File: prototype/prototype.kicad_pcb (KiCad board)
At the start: 4 copper layers, 78.7 x 63.5 mm, 47 parts, among them P1 CONN_25X2, P2 CONN_25X2, P3 VGACONN, U1 MC68SEC000, U2 FLASHROM_512K_16, U3 RAM_512K_16, U4 RAM_512K_16

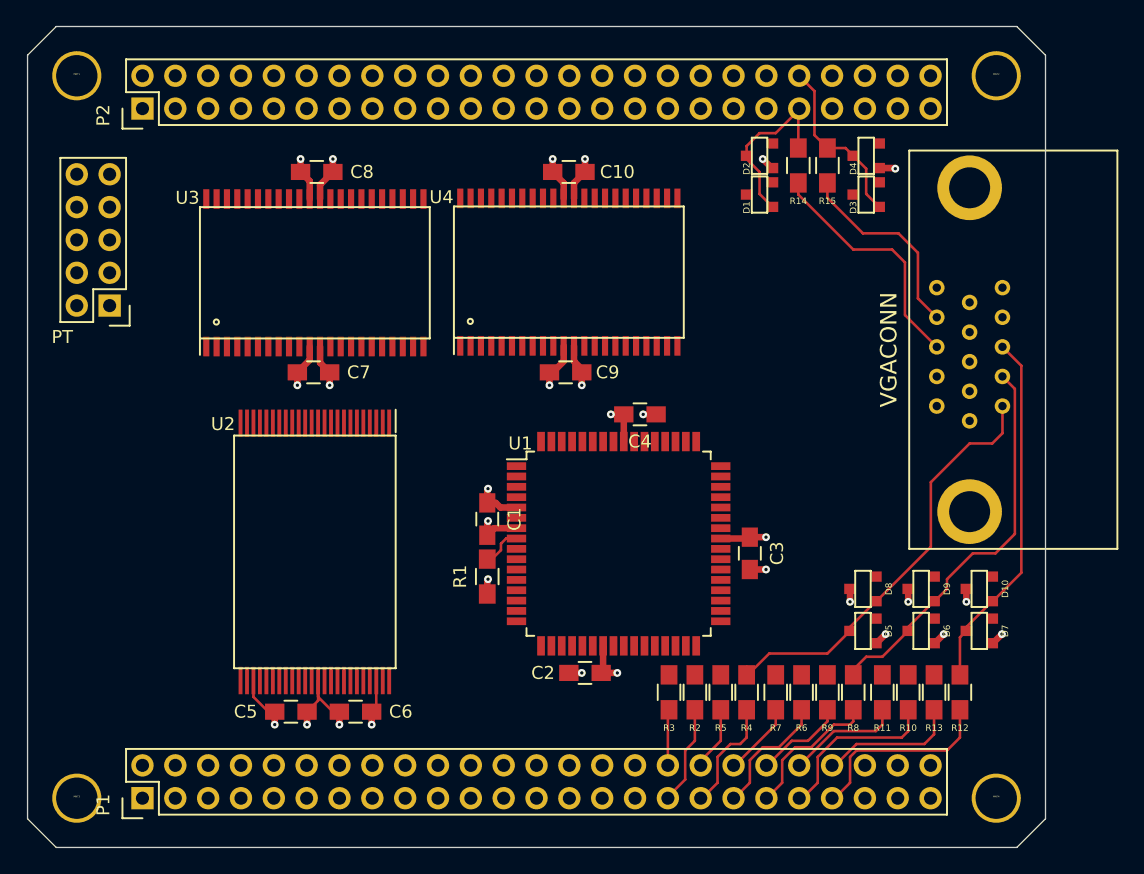
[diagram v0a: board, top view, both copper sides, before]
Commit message: Break out all of the chip signal pads to vias.
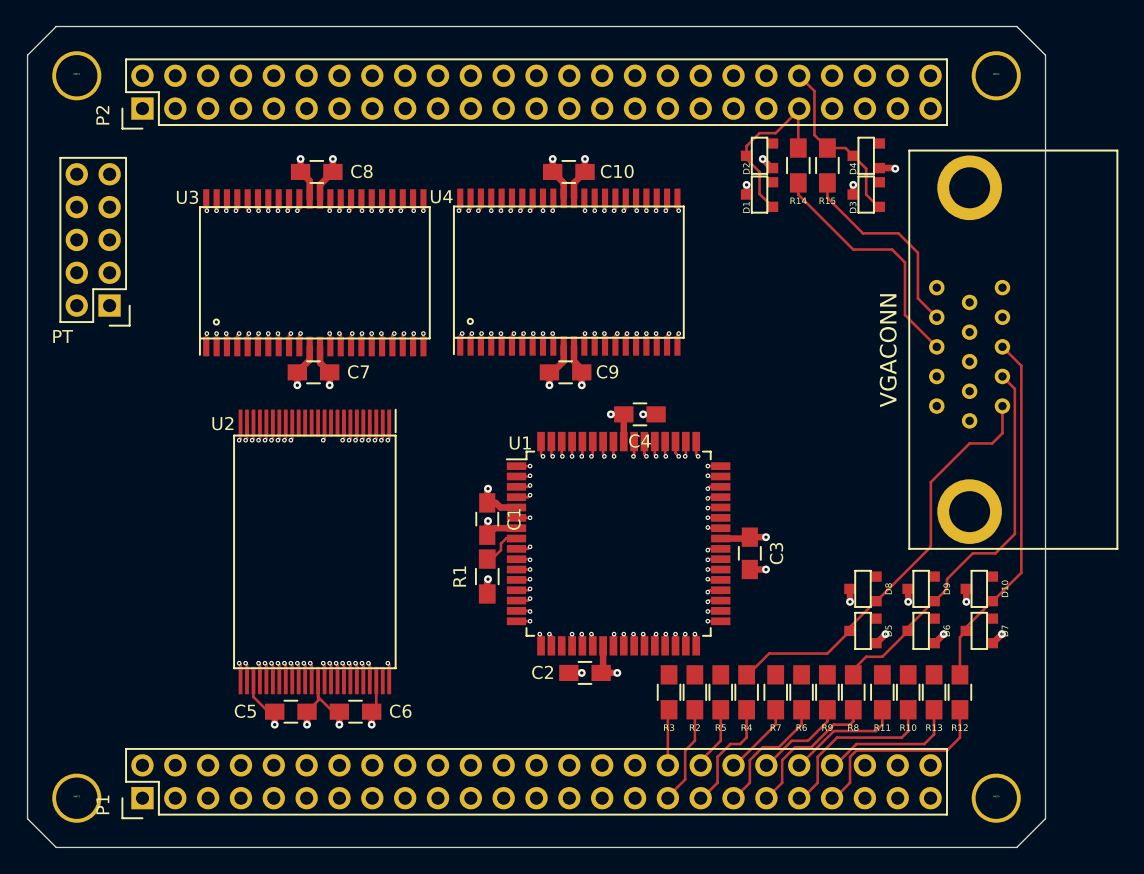
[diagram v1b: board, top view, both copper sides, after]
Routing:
- net D6: track 0.00 -> 4.61 mm, vias 0 -> 4
- net D7: track 0.00 -> 4.61 mm, vias 0 -> 4
- net D2: track 0.00 -> 4.59 mm, vias 0 -> 4
- net D3: track 0.00 -> 4.59 mm, vias 0 -> 4
- net D9: track 0.00 -> 4.58 mm, vias 0 -> 4
- net D5: track 0.00 -> 4.55 mm, vias 0 -> 4
- net D1: track 0.00 -> 4.55 mm, vias 0 -> 4
- net D4: track 0.00 -> 4.55 mm, vias 0 -> 4
- net D0: track 0.00 -> 4.53 mm, vias 0 -> 4
- net D11: track 0.00 -> 4.49 mm, vias 0 -> 4
- net D8: track 0.00 -> 4.47 mm, vias 0 -> 4
- net D10: track 0.00 -> 4.45 mm, vias 0 -> 4
- net D14: track 0.00 -> 4.41 mm, vias 0 -> 4
- net D15: track 0.00 -> 4.35 mm, vias 0 -> 4
- net D12: track 0.00 -> 4.33 mm, vias 0 -> 4
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
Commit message: Address line traces from Mojo to 68000.
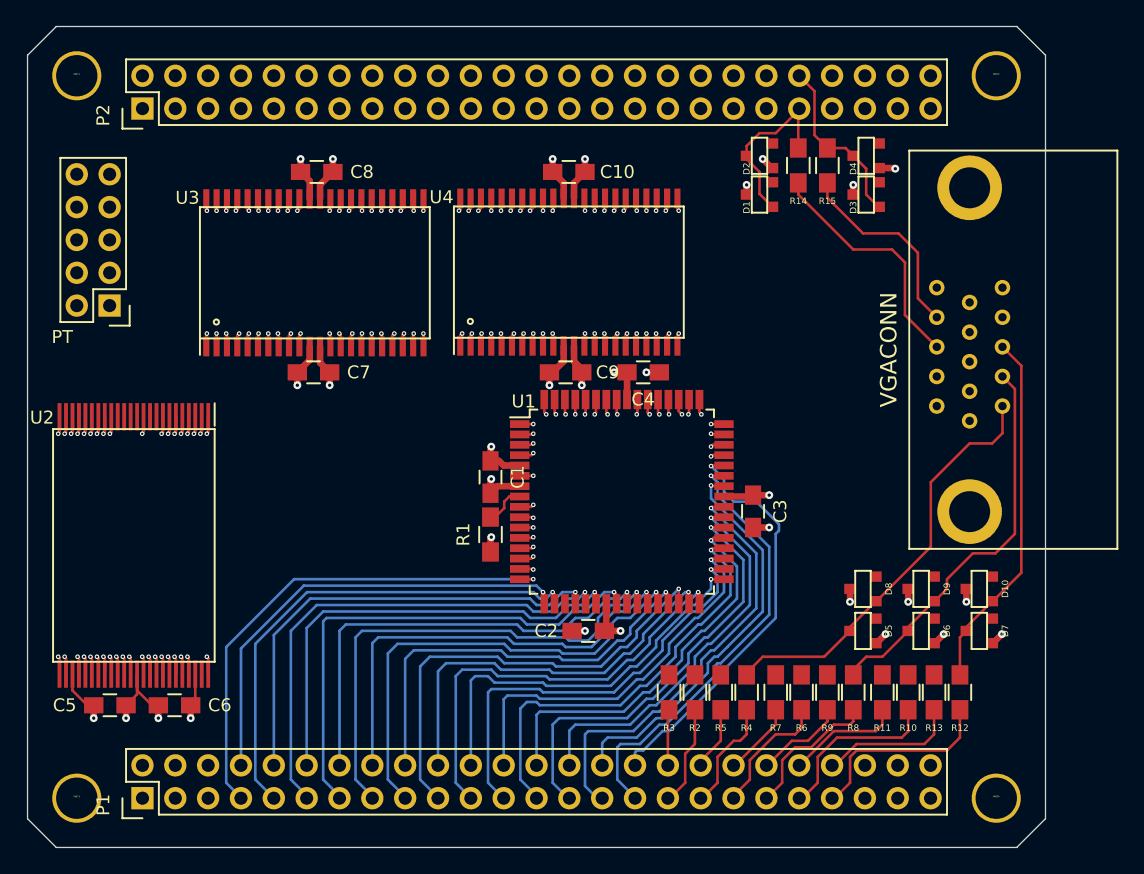
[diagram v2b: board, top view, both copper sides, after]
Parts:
- moved U2 14.0 mm to (120.6, 101.1)
- moved C5 14.0 mm to (118.8, 113.5)
- moved C6 14.0 mm to (123.8, 113.5)
- moved C1 3.26 mm to (148.2, 95.8)
- moved C2 3.26 mm to (155.8, 107.7)
- moved C3 3.26 mm to (168.5, 98.5)
- moved C4 3.26 mm to (160.0, 87.7)
- moved R1 3.26 mm to (148.2, 100.3)
- moved U1 3.26 mm to (158.4, 97.7)
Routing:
- net FC2: track 1.05 -> 39.3 mm
- net A4: track 4.28 -> 42.5 mm
- net A2: track 4.30 -> 42.2 mm
- net FC0: track 0.97 -> 38.6 mm
- net A6: track 4.20 -> 41.7 mm
- net A8: track 4.27 -> 40.0 mm
- net A1: track 4.31 -> 39.5 mm
- net FC1: track 0.95 -> 36.1 mm
- net A3: track 4.30 -> 38.8 mm
- net A10: track 4.16 -> 38.6 mm
- net A5: track 4.30 -> 38.6 mm
- net LA22: track 1.00 -> 34.7 mm
- net A7: track 4.22 -> 37.7 mm
- net LA20: track 1.04 -> 33.8 mm
- net LA12: track 0.95 -> 33.2 mm
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
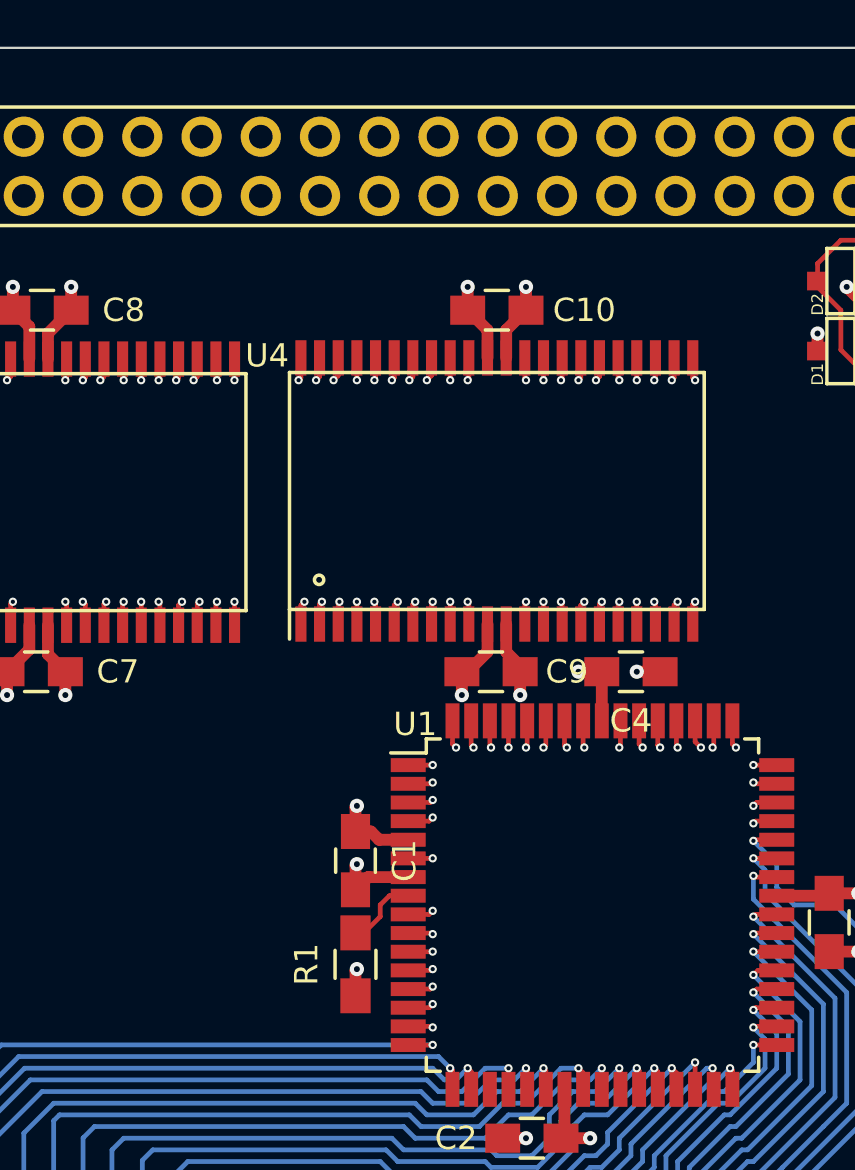
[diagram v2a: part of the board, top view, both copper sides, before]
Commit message: More PCB traces.
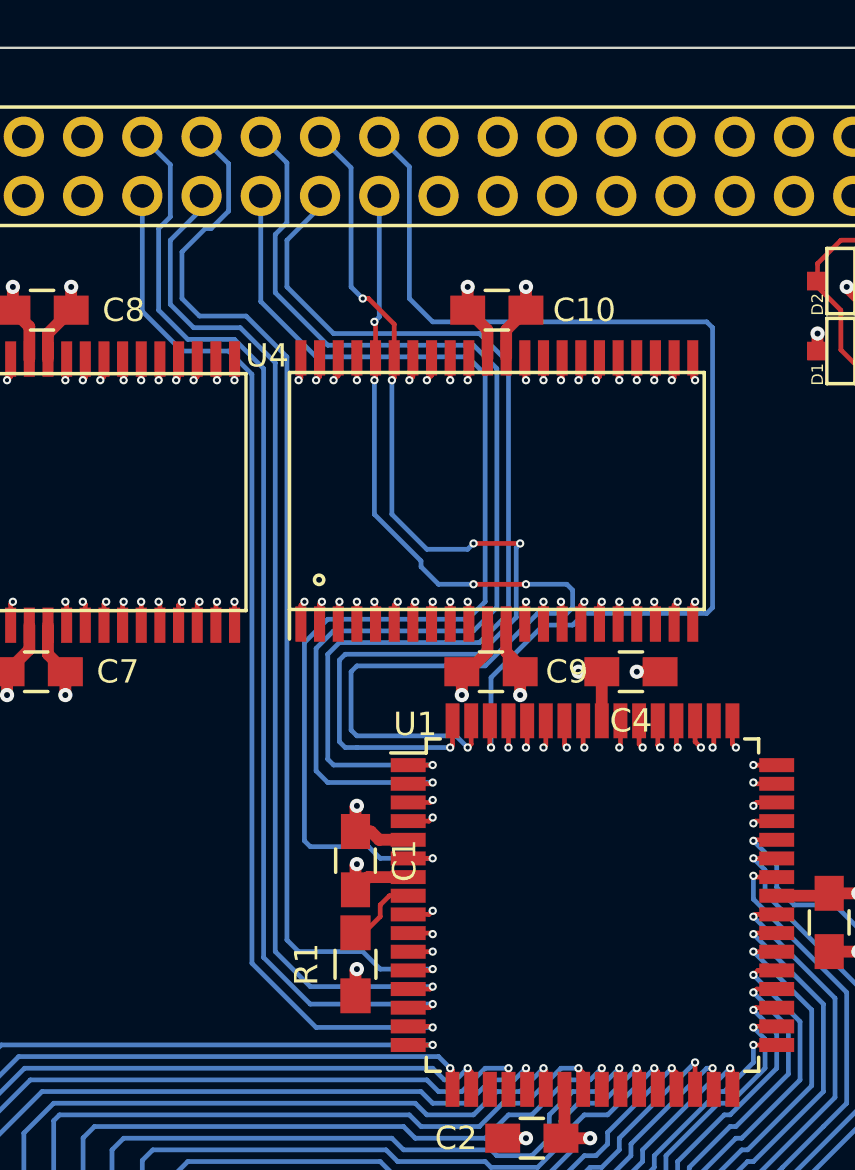
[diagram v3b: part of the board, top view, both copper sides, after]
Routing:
- net CLK: track 1.05 -> 49.0 mm
- net ~DTACK: track 1.07 -> 48.5 mm
- net ~IPL1: track 1.11 -> 48.1 mm
- net ~AS: track 1.17 -> 47.9 mm
- net ~BERR: track 1.07 -> 46.8 mm
- net ~IPL0: track 1.07 -> 46.0 mm
- net R/~W: track 1.05 -> 44.7 mm
- net ~IPL2: track 1.09 -> 44.5 mm
- net ~LDS: track 3.13 -> 46.0 mm, vias 3 -> 6
- net ~UDS: track 3.11 -> 45.1 mm, vias 3 -> 6

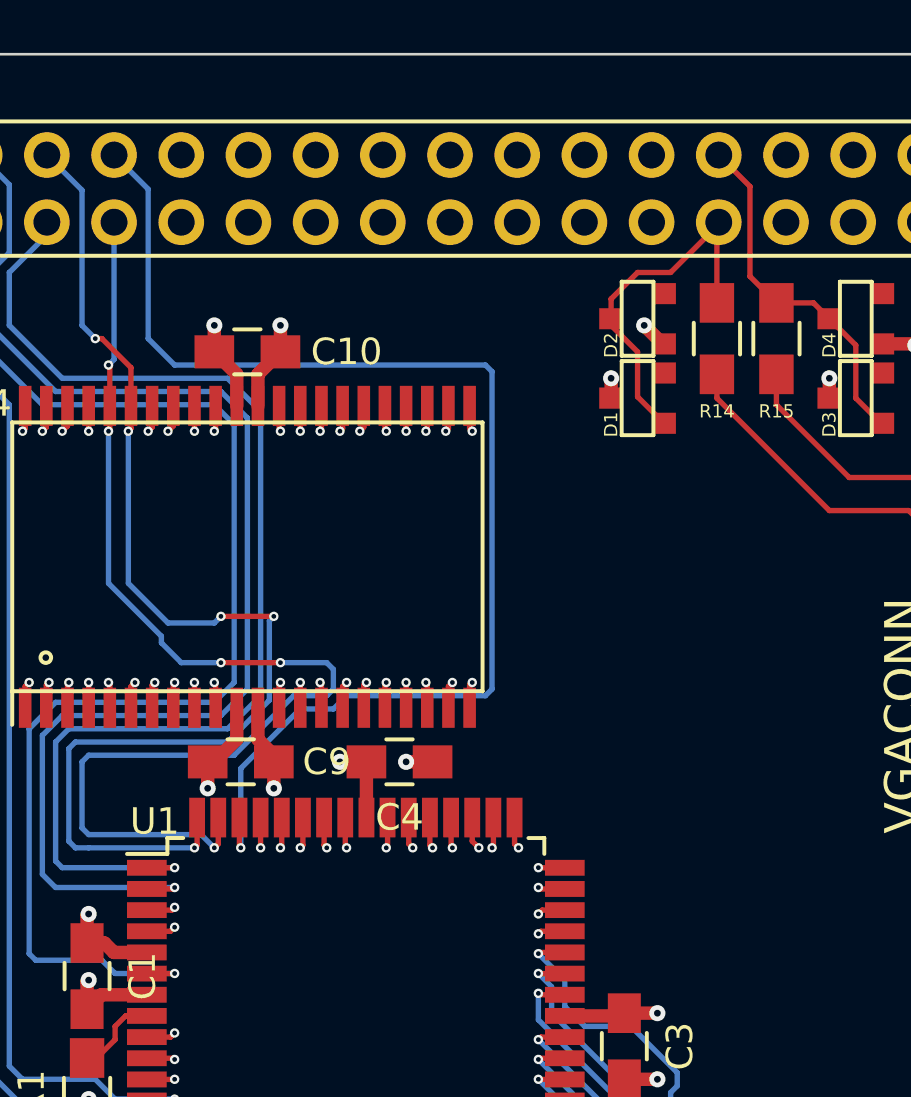
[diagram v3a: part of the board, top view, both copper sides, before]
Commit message: Data bus traces to the CPU, and others.
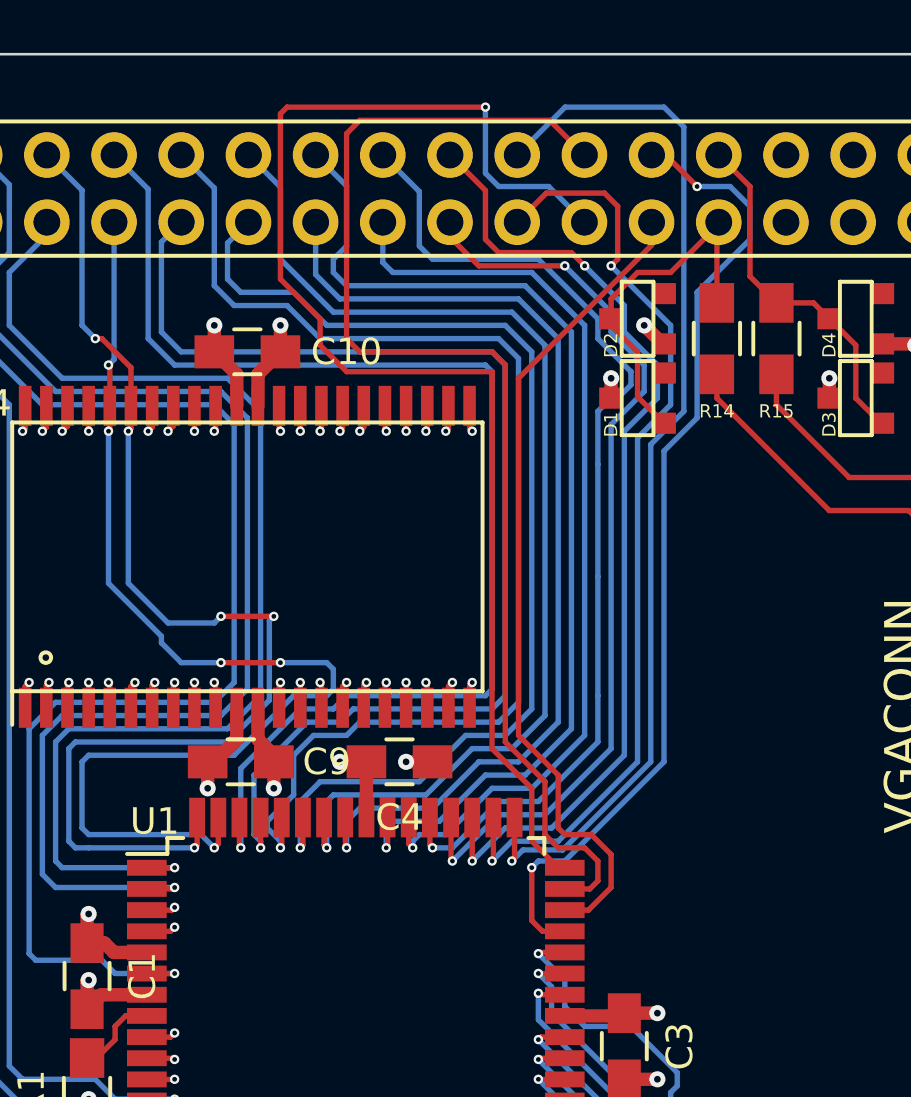
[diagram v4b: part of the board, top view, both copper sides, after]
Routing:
- net D12: track 4.33 -> 54.5 mm
- net D13: track 4.31 -> 50.1 mm, vias 4 -> 3
- net D1: track 4.55 -> 49.1 mm
- net D0: track 4.53 -> 48.6 mm
- net D3: track 4.59 -> 45.7 mm
- net D2: track 4.59 -> 45.2 mm
- net D5: track 4.55 -> 43.9 mm
- net D11: track 4.49 -> 43.7 mm
- net D4: track 4.55 -> 41.8 mm
- net D7: track 4.61 -> 41.6 mm
- net D15: track 4.35 -> 41.3 mm, vias 4 -> 5
- net D9: track 4.58 -> 40.4 mm, vias 4 -> 5
- net D10: track 4.45 -> 39.0 mm, vias 4 -> 5
- net D6: track 4.61 -> 38.7 mm
- net D8: track 4.47 -> 38.1 mm, vias 4 -> 5
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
